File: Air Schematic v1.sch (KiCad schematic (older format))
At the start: 19 parts

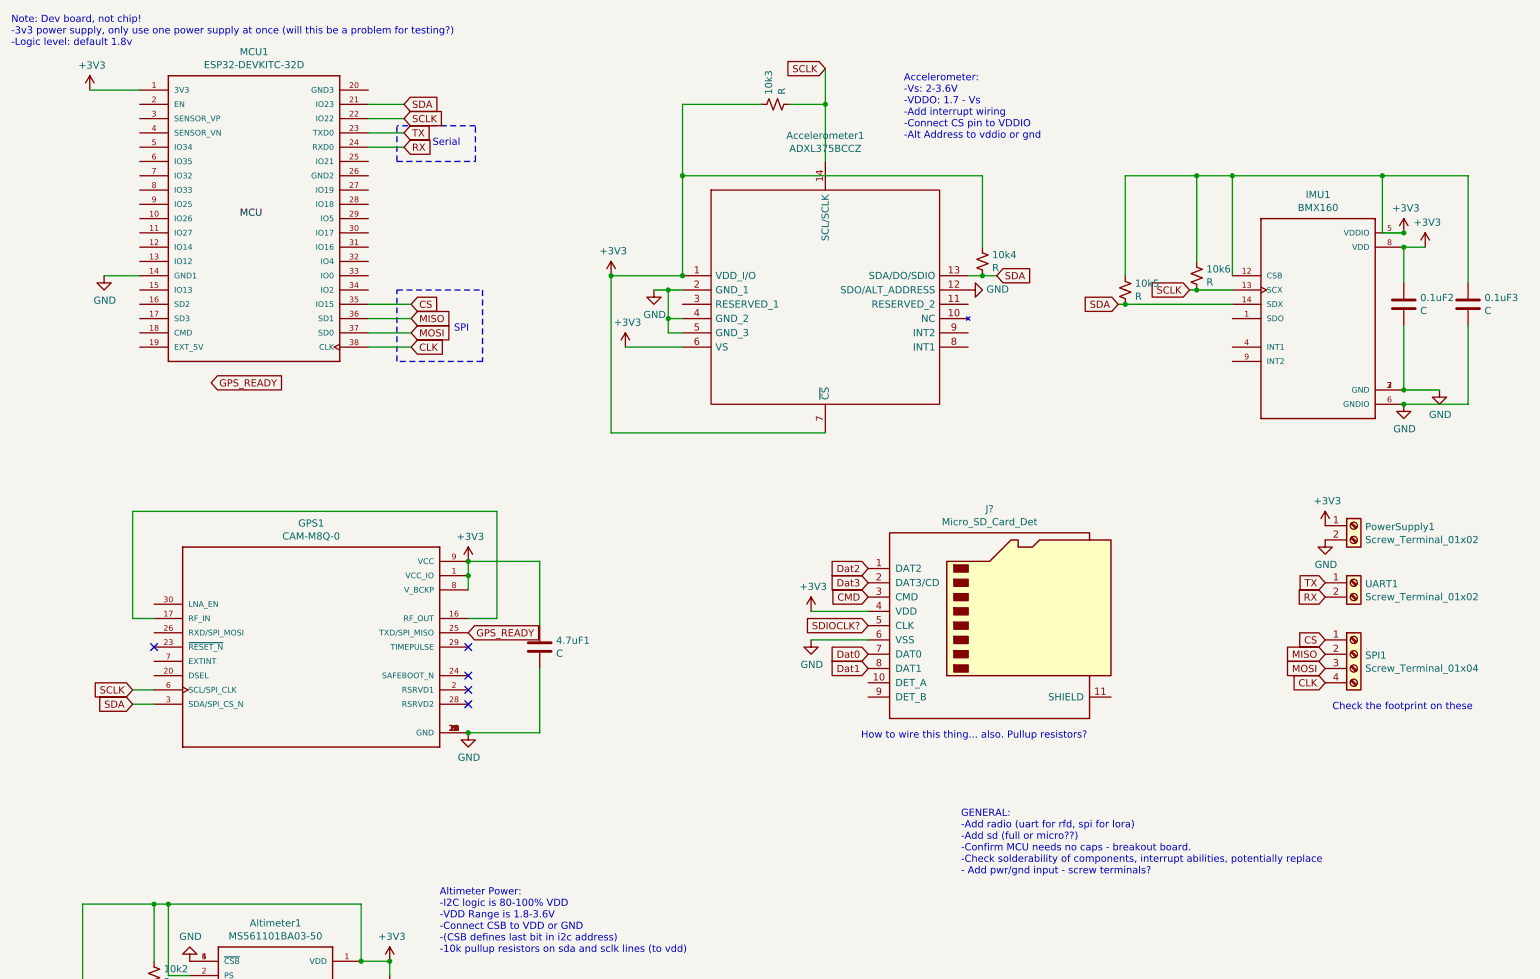
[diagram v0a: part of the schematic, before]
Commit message: Added footprints, initial pcb layouts
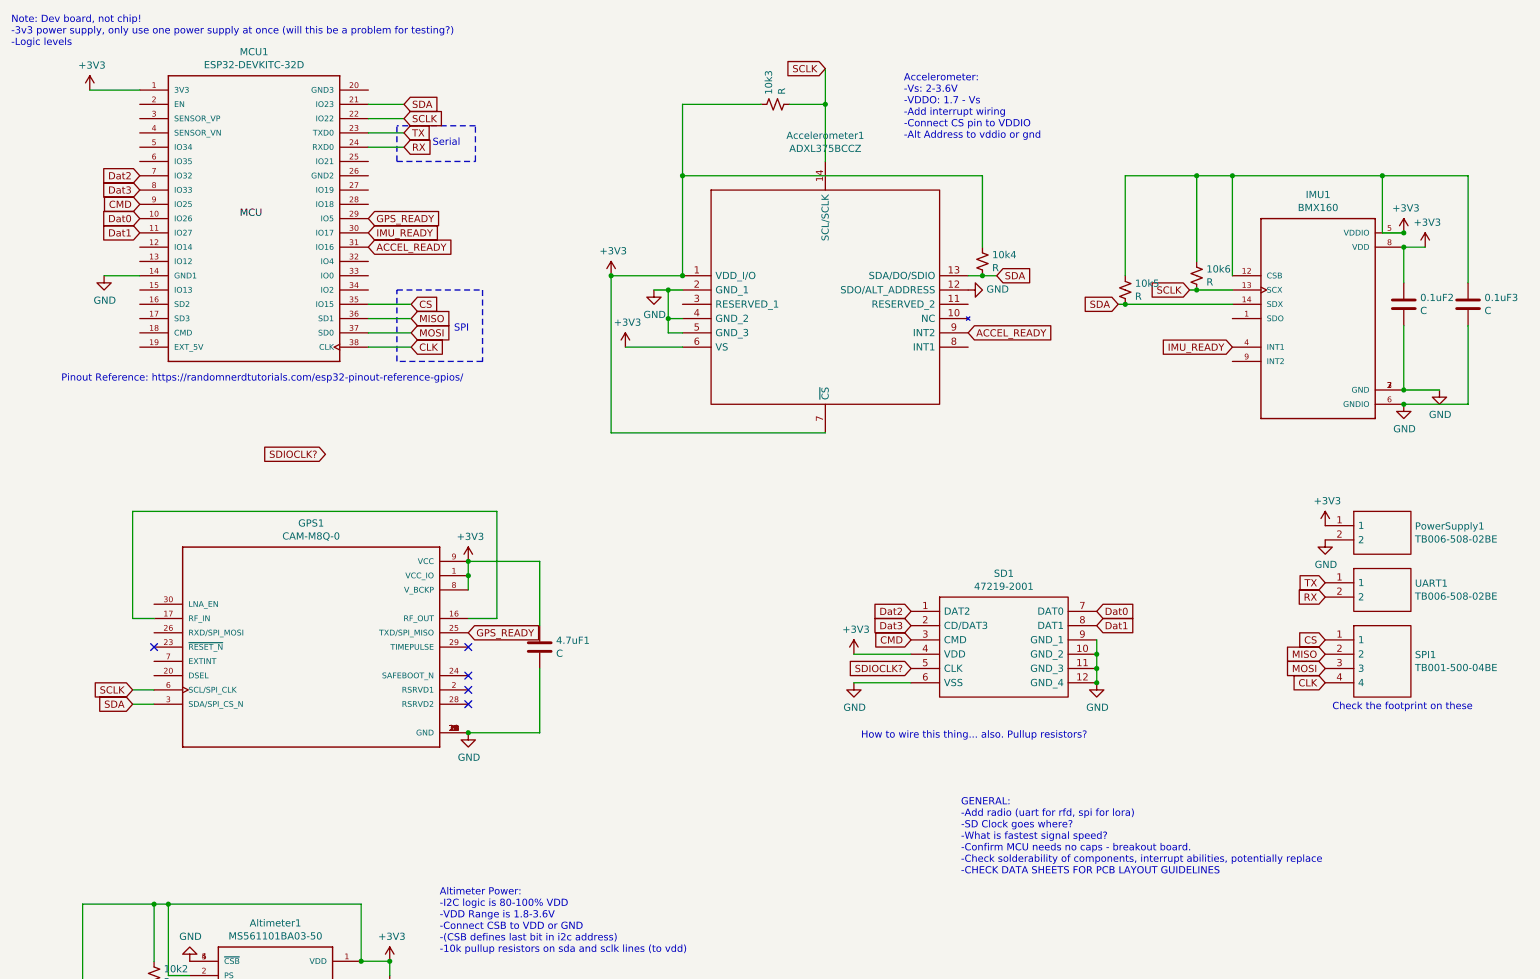
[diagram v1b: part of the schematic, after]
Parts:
- removed J?: Micro_SD_Card_Det, symbol Connector:Micro_SD_Card_Det
- removed PowerSupply1, UART1: Screw_Terminal_01x02, symbol Connector:Screw_Terminal_01x02
- removed SPI1: Screw_Terminal_01x04, symbol Connector:Screw_Terminal_01x04
- added PowerSupply1, UART1: TB006-508-02BE, SamacSys_Parts:TB00650802BE, symbol SamacSys_Parts:TB006-508-02BE
- added SD1: 47219-2001, SamacSys_Parts:472192001, symbol SamacSys_Parts:47219-2001
- added SPI1: TB001-500-04BE, SamacSys_Parts:TB00150004BE, symbol SamacSys_Parts:TB001-500-04BE
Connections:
- net +3V3: now also PowerSupply1.1, SD1.4 (VDD)
- net CLK: now also SPI1.4
- net CMD: now also MCU1.9 (IO25), SD1.3 (CMD)
- net CS: now also SPI1.1
- net Dat0: now also MCU1.10 (IO26), SD1.7 (DAT0)
- net Dat1: now also MCU1.11 (IO27), SD1.8 (DAT1)
- net Dat2: now also MCU1.7 (IO32), SD1.1 (DAT2)
- net Dat3: now also MCU1.8 (IO33), SD1.2 (CD/DAT3)
- net GND: now also PowerSupply1.2, SD1.10 (GND_2), SD1.11 (GND_3), SD1.12 (GND_4), SD1.6 (VSS), SD1.9 (GND_1)
- net GPS_READY: now also MCU1.29 (IO5)
- net MISO: now also SPI1.2
- net MOSI: now also SPI1.3
- net RX: now also UART1.2
- net SDIOCLK?: now also SD1.5 (CLK)
- net TX: now also UART1.1
- net IMU_READY: now reaches MCU1.30 (IO17)
- net IMU_READY: now also IMU1.4 (INT1)
- net ACCEL_READY: now reaches MCU1.31 (IO16)
- net ACCEL_READY: now also Accelerometer1.9 (INT2)
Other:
- note added: "GENERAL:\n-Add radio (uart for rfd, spi for lora)\n-SD Clock goes where?\n-What is fastest signal speed?\n-Confirm MCU needs no caps - breakout board.\n-Check solderability of components, interrupt abilities, potentially replace\n-CHECK DATA SHEETS FOR PCB LAYOUT GUIDELINES"
- note added: "Note: Dev board, not chip!\n-3v3 power supply, only use one power supply at once (will this be a problem for testing?)\n-Logic levels"
- note added: "Pinout Reference: https://randomnerdtutorials.com/esp32-pinout-reference-gpios/"
- note removed: "GENERAL:\n-Add radio (uart for rfd, spi for lora)\n-Add sd (full or micro??)\n-Confirm MCU needs no caps - breakout board.\n-Check solderability of components, interrupt abilities, potentially replace\n- Add pwr/gnd input - screw terminals?"
- note removed: "Note: Dev board, not chip!\n-3v3 power supply, only use one power supply at once (will this be a problem for testing?)\n-Logic level: default 1.8v"
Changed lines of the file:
@@
 SDA
 Text Notes 7150 6500 0    50   ~ 0
-GENERAL:\n-Add radio (uart for rfd, spi for lora)\n-Add sd (full or micro??)\n-Confirm MCU needs no caps - breakout board.\n-Check solderability of components, interrupt abilities, potentially replace\n- Add pwr/gnd input - screw terminals?
+GENERAL:\n-Add radio (uart for rfd, spi for lora)\n-SD Clock goes where?\n-What is fastest signal speed?\n-Confirm MCU needs no caps - breakout board.\n-Check solderability of components, interrupt abilities, potentially replace\n-CHECK DATA SHEETS FOR PCB LAYOUT GUIDELINES
 $Comp
 L power:+3V3 #PWR0104
@@
 Altimeter Power:\n-I2C logic is 80-100% VDD\n-VDD Range is 1.8-3.6V\n-Connect CSB to VDD or GND\n-(CSB defines last bit in i2c address)\n-10k pullup resistors on sda and sclk lines (to vdd)
 Text Notes 500  700  0    50   ~ 0
-Note: Dev board, not chip!\n-3v3 power supply, only use one power supply at once (will this be a problem for testing?)\n-Logic level: default 1.8v
+Note: Dev board, not chip!\n-3v3 power supply, only use one power supply at once (will this be a problem for testing?)\n-Logic levels
 Wire Wire Line
 	1750 7200 1600 7200
@@
 Text GLabel 3700 4800 2    50   Input ~ 0
 GPS_READY
-Text GLabel 1900 3050 2    50   Input ~ 0
+Text GLabel 3000 1900 2    50   Input ~ 0
 GPS_READY
 Wire Wire Line
@@
 	1    0    0    -1
 $EndComp
-$Comp
-L Connector:Screw_Terminal_01x02 PowerSupply1
-U 1 1 5F448AC7
-P 9900 4050
-F 0 "PowerSupply1" H 9980 4042 50  0000 L CNN
-F 1 "Screw_Terminal_01x02" H 9980 3951 50  0000 L CNN
-F 2 "" H 9900 4050 50  0001 C CNN
-F 3 "~" H 9900 4050 50  0001 C CNN
-	1    9900 4050
-	1    0    0    -1
-$EndComp
-$Comp
-L Connector:Screw_Terminal_01x02 UART1
-U 1 1 5F44AAAB
-P 9900 4450
-F 0 "UART1" H 9980 4442 50  0000 L CNN
-F 1 "Screw_Terminal_01x02" H 9980 4351 50  0000 L CNN
-F 2 "" H 9900 4450 50  0001 C CNN
-F 3 "~" H 9900 4450 50  0001 C CNN
-	1    9900 4450
-	1    0    0    -1
-$EndComp
-$Comp
-L Connector:Screw_Terminal_01x04 SPI1
-U 1 1 5F44C81C
-P 9900 4950
-F 0 "SPI1" H 9980 4942 50  0000 L CNN
-F 1 "Screw_Terminal_01x04" H 9980 4851 50  0000 L CNN
-F 2 "" H 9900 4950 50  0001 C CNN
-F 3 "~" H 9900 4950 50  0001 C CNN
-	1    9900 4950
-	1    0    0    -1
-$EndComp
 Wire Wire Line
 	1400 2300 1150 2300
@@
 	1    0    0    -1
 $EndComp
-Text GLabel 9700 4850 0    50   Input ~ 0
-CS
-Text GLabel 9700 4950 0    50   Input ~ 0
-MISO
-Text GLabel 9700 5050 0    50   Input ~ 0
-MOSI
-Text GLabel 9700 5150 0    50   Input ~ 0
-CLK
 Text GLabel 9700 4450 0    50   Input ~ 0
 TX
 Text GLabel 9700 4550 0    50   Input ~ 0
 RX
-Text Notes 9750 5350 0    50   ~ 0
-Check the footprint on these
-$Comp
-L Connector:Micro_SD_Card_Det J?
-U 1 1 5F46BD62
-P 7400 4750
-F 0 "J?" H 7350 5567 50  0000 C CNN
-F 1 "Micro_SD_Card_Det" H 7350 5476 50  0000 C CNN
-F 2 "" H 9450 5450 50  0001 C CNN
-F 3 "https://www.hirose.com/product/en/download_file/key_name/DM3/category/Catalog/doc_file_id/49662/?file_category_id=4&item_id=195&is_series=1" H 7400 4850 50  0001 C CNN
-	1    7400 4750
-	1    0    0    -1
-$EndComp
-$Comp
-L power:+3V3 #PWR?
+$Comp
+L power:+3V3 #PWR01
 U 1 1 5F470C0E
-P 6100 4650
-F 0 "#PWR?" H 6100 4500 50  0001 C CNN
-F 1 "+3V3" H 6115 4823 50  0000 C CNN
-F 2 "" H 6100 4650 50  0001 C CNN
-F 3 "" H 6100 4650 50  0001 C CNN
-	1    6100 4650
-	1    0    0    -1
-$EndComp
-$Comp
-L power:GND #PWR?
+P 6400 4950
+F 0 "#PWR01" H 6400 4800 50  0001 C CNN
+F 1 "+3V3" H 6415 5123 50  0000 C CNN
+F 2 "" H 6400 4950 50  0001 C CNN
+F 3 "" H 6400 4950 50  0001 C CNN
+	1    6400 4950
+	1    0    0    -1
+$EndComp
+$Comp
+L power:GND #PWR02
 U 1 1 5F473626
-P 6100 4850
-F 0 "#PWR?" H 6100 4600 50  0001 C CNN
-F 1 "GND" H 6105 4677 50  0000 C CNN
-F 2 "" H 6100 4850 50  0001 C CNN
-F 3 "" H 6100 4850 50  0001 C CNN
-	1    6100 4850
-	1    0    0    -1
-$EndComp
-Text GLabel 6500 4950 0    50   Input ~ 0
+P 6400 5150
+F 0 "#PWR02" H 6400 4900 50  0001 C CNN
+F 1 "GND" H 6405 4977 50  0000 C CNN
+F 2 "" H 6400 5150 50  0001 C CNN
+F 3 "" H 6400 5150 50  0001 C CNN
+	1    6400 5150
+	1    0    0    -1
+$EndComp
+Text GLabel 8100 4650 2    50   Input ~ 0
 Dat0
-Text GLabel 6500 5050 0    50   Input ~ 0
+Text GLabel 8100 4750 2    50   Input ~ 0
 Dat1
-Text GLabel 6500 4350 0    50   Input ~ 0
+Text GLabel 6800 4650 0    50   Input ~ 0
 Dat2
-Text GLabel 6500 4450 0    50   Input ~ 0
+Text GLabel 6800 4750 0    50   Input ~ 0
 Dat3
 Wire Wire Line
-	6100 4850 6500 4850
-Wire Wire Line
-	6100 4650 6500 4650
-Text GLabel 6500 4750 0    50   Input ~ 0
+	6400 5150 6800 5150
+Wire Wire Line
+	6400 4950 6800 4950
+Text GLabel 6800 5050 0    50   Input ~ 0
 SDIOCLK?
-Text GLabel 6500 4550 0    50   Input ~ 0
+Text GLabel 6800 4850 0    50   Input ~ 0
 CMD
 Text Notes 6450 5550 0    50   ~ 0
 How to wire this thing... also. Pullup resistors?
+Text GLabel 1400 1600 0    50   Input ~ 0
+Dat2
+Text GLabel 1400 1700 0    50   Input ~ 0
+Dat3
+Text GLabel 1400 1800 0    50   Input ~ 0
+CMD
+Text GLabel 1400 1900 0    50   Input ~ 0
+Dat0
+Text GLabel 1400 2000 0    50   Input ~ 0
+Dat1
+Text GLabel 2700 3550 0    50   Input ~ 0
+SDIOCLK?
+Text GLabel 3000 2000 2    50   Input ~ 0
+IMU_READY
+Text GLabel 9050 2800 0    50   Input ~ 0
+IMU_READY
+Text GLabel 7200 2700 2    50   Input ~ 0
+ACCEL_READY
+Text GLabel 3000 2100 2    50   Input ~ 0
+ACCEL_READY
+Text Notes 850  3050 0    50   ~ 0
+Pinout Reference: https://randomnerdtutorials.com/esp32-pinout-reference-gpios/
+$Comp
+L SamacSys_Parts:47219-2001 SD1
+U 1 1 5F4D7F0F
+P 6800 4650
+F 0 "SD1" H 7450 4915 50  0000 C CNN
+F 1 "47219-2001" H 7450 4824 50  0000 C CNN
+F 2 "SamacSys_Parts:472192001" H 7950 4750 50  0001 L CNN
+F 3 "http://www.molex.com/molex/products/datasheet.jsp?part=active/0472192001_MEMORY_CARD_SOCKET.xml&channel=Products&Lang=en-US" H 7950 4650 50  0001 L CNN
+F 4 "Molex 47219 Series 8 Way Horizontal Hinged Micro SD Memory Card Connector with Solder Termination" H 7950 4550 50  0001 L CNN "Description"
+F 5 "" H 7950 4450 50  0001 L CNN "Height"
+F 6 "538-47219-2001" H 7950 4350 50  0001 L CNN "Mouser Part Number"
+F 7 "https://www.mouser.co.uk/ProductDetail/Molex/47219-2001?qs=6kT3pPPHxnVaoXw6Dd7beQ%3D%3D" H 7950 4250 50  0001 L CNN "Mouser Price/Stock"
+F 8 "Molex" H 7950 4150 50  0001 L CNN "Manufacturer_Name"
+F 9 "47219-2001" H 7950 4050 50  0001 L CNN "Manufacturer_Part_Number"
+	1    6800 4650
+	1    0    0    -1
+$EndComp
+$Comp
+L power:GND #PWR03
+U 1 1 5F4E851D
+P 8100 5150
+F 0 "#PWR03" H 8100 4900 50  0001 C CNN
+F 1 "GND" H 8105 4977 50  0000 C CNN
+F 2 "" H 8100 5150 50  0001 C CNN
+F 3 "" H 8100 5150 50  0001 C CNN
+	1    8100 5150
+	1    0    0    -1
+$EndComp
+Wire Wire Line
+	8100 5050 8100 5150
+Connection ~ 8100 5050
+Connection ~ 8100 4950
+Wire Wire Line
+	8100 4950 8100 5050
+Connection ~ 8100 5150
+Wire Wire Line
+	8100 4850 8100 4950
+Text Notes 9750 5350 0    50   ~ 0
+Check the footprint on these
+Text GLabel 9700 5150 0    50   Input ~ 0
+CLK
+Text GLabel 9700 5050 0    50   Input ~ 0
+MOSI
+Text GLabel 9700 4950 0    50   Input ~ 0
+MISO
+Text GLabel 9700 4850 0    50   Input ~ 0
+CS
+$Comp
+L SamacSys_Parts:TB001-500-04BE SPI1
+U 1 1 5F541036
+P 9700 4850
+F 0 "SPI1" H 10328 4746 50  0000 L CNN
+F 1 "TB001-500-04BE" H 10328 4655 50  0000 L CNN
+F 2 "SamacSys_Parts:TB00150004BE" H 10350 4950 50  0001 L CNN
+F 3 "https://componentsearchengine.com/Datasheets/1/TB001-500-04BE.pdf" H 10350 4850 50  0001 L CNN
+F 4 "Fixed Terminal Blocks Terminal block, screw type, 5.00, horizontal, 4 poles, CUI Blue, slotted screw, PCB mount" H 10350 4750 50  0001 L CNN "Description"
+F 5 "12.9" H 10350 4650 50  0001 L CNN "Height"
+F 6 "490-TB001-500-04BE" H 10350 4550 50  0001 L CNN "Mouser Part Number"
+F 7 "https://www.mouser.co.uk/ProductDetail/CUI-Devices/TB001-500-04BE?qs=vLWxofP3U2xFd1xqNcHXZA%3D%3D" H 10350 4450 50  0001 L CNN "Mouser Price/Stock"
+F 8 "CUI Devices" H 10350 4350 50  0001 L CNN "Manufacturer_Name"
+F 9 "TB001-500-04BE" H 10350 4250 50  0001 L CNN "Manufacturer_Part_Number"
+	1    9700 4850
+	1    0    0    -1
+$EndComp
+$Comp
+L SamacSys_Parts:TB006-508-02BE UART1
+U 1 1 5F5421F0
+P 9700 4450
+F 0 "UART1" H 10328 4446 50  0000 L CNN
+F 1 "TB006-508-02BE" H 10328 4355 50  0000 L CNN
+F 2 "SamacSys_Parts:TB00650802BE" H 10350 4550 50  0001 L CNN
+F 3 "" H 10350 4450 50  0001 L CNN
+F 4 "Fixed Terminal Blocks screw type, 5.08 , horizontal, 2 poles, CUI Blue, slotted screw, PCB mount" H 10350 4350 50  0001 L CNN "Description"
+F 5 "10.4" H 10350 4250 50  0001 L CNN "Height"
+F 6 "490-TB006-508-02BE" H 10350 4150 50  0001 L CNN "Mouser Part Number"
+F 7 "https://www.mouser.co.uk/ProductDetail/CUI-Devices/TB006-508-02BE?qs=vLWxofP3U2wEdOVV%2FaT04w%3D%3D" H 10350 4050 50  0001 L CNN "Mouser Price/Stock"
+F 8 "CUI Devices" H 10350 3950 50  0001 L CNN "Manufacturer_Name"
+F 9 "TB006-508-02BE" H 10350 3850 50  0001 L CNN "Manufacturer_Part_Number"
+	1    9700 4450
+	1    0    0    -1
+$EndComp
+$Comp
+L SamacSys_Parts:TB006-508-02BE PowerSupply1
+U 1 1 5F54DCFB
+P 9700 4050
+F 0 "PowerSupply1" H 10328 4046 50  0000 L CNN
+F 1 "TB006-508-02BE" H 10328 3955 50  0000 L CNN
+F 2 "SamacSys_Parts:TB00650802BE" H 10350 4150 50  0001 L CNN
+F 3 "" H 10350 4050 50  0001 L CNN
+F 4 "Fixed Terminal Blocks screw type, 5.08 , horizontal, 2 poles, CUI Blue, slotted screw, PCB mount" H 10350 3950 50  0001 L CNN "Description"
+F 5 "10.4" H 10350 3850 50  0001 L CNN "Height"
+F 6 "490-TB006-508-02BE" H 10350 3750 50  0001 L CNN "Mouser Part Number"
+F 7 "https://www.mouser.co.uk/ProductDetail/CUI-Devices/TB006-508-02BE?qs=vLWxofP3U2wEdOVV%2FaT04w%3D%3D" H 10350 3650 50  0001 L CNN "Mouser Price/Stock"
+F 8 "CUI Devices" H 10350 3550 50  0001 L CNN "Manufacturer_Name"
+F 9 "TB006-508-02BE" H 10350 3450 50  0001 L CNN "Manufacturer_Part_Number"
+	1    9700 4050
+	1    0    0    -1
+$EndComp
 $EndSCHEMATC

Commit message: Switched out altimeter and IMU
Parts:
- added 0.1uF4, 0.1uF5: C, Capacitor_SMD:C_0603_1608Metric, symbol Device:C
- added 10k7, 10k8: R, Resistor_SMD:R_0603_1608Metric, symbol Device:R_Small_US
- added IC1: BMX055, BMX055:BMX055, symbol BMX055:BMX055
- added MS561101BA03_Breakout1: Altimeter, MS561101BA03-50:Inexact_Altimeter_Breakout, symbol New_Parts:Altimeter
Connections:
- net labels removed: SDIOCLK?
- wire segments 83 -> 94
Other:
- note added: "GENERAL:\n-Add radio (uart for rfd, spi for lora)\n-SD Clock goes where?\n-What is fastest signal speed?\n-Confirm MCU needs no caps - breakout board.\n-Check solderability of components, interrupt abilities, potentially replace\n-CHECK DATA SHEETS FOR PCB LAYOUT GUIDELINES\n-Keepouts for decoupling caps\n-GPS pull up resistors for i2c\n-Make room for gps\n-Add antenna output just in case"
- note added: "Note: Dev board, not chip!\n-3v3 power supply, only use one power supply at once (will this be a problem for testing?)\n-Logic levels: default 3.3v operation"
- note removed: "GENERAL:\n-Add radio (uart for rfd, spi for lora)\n-SD Clock goes where?\n-What is fastest signal speed?\n-Confirm MCU needs no caps - breakout board.\n-Check solderability of components, interrupt abilities, potentially replace\n-CHECK DATA SHEETS FOR PCB LAYOUT GUIDELINES"
- note removed: "Note: Dev board, not chip!\n-3v3 power supply, only use one power supply at once (will this be a problem for testing?)\n-Logic levels"
- moved on the sheet: 0.1uF1, 0.1uF2, 0.1uF3, 10k1, 10k2, 10k5, 10k6, Altimeter1, IMU1
